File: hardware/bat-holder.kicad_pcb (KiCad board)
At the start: 2 copper layers, 85 x 56 mm, 113 parts, among them J101 BAT_1049P, J102 USB-A, K101 NTC, P101 BOOT, P102 DEBUG, P103 CON-SENSOR2, P104 C, P105 5V Out, P201 Input, Q101 BC846, Q102 BC846, Q103 DMP2035UVTQ, Q104 DMP2035UVTQ, Q201 Si4447ADY, U101 XMC1XXX24, U102 AP9211, U103 MAX17260_LS, U104 DRILL, U105 DRILL, U106 DRILL, U107 DRILL, U108 DRILL, U109 DRILL, U110 DRILL, U111 DRILL, U112 AP7333-33SA, U201 TPS61088RHL, U202 BD906XX-C-HRP7, U203 AAT3620

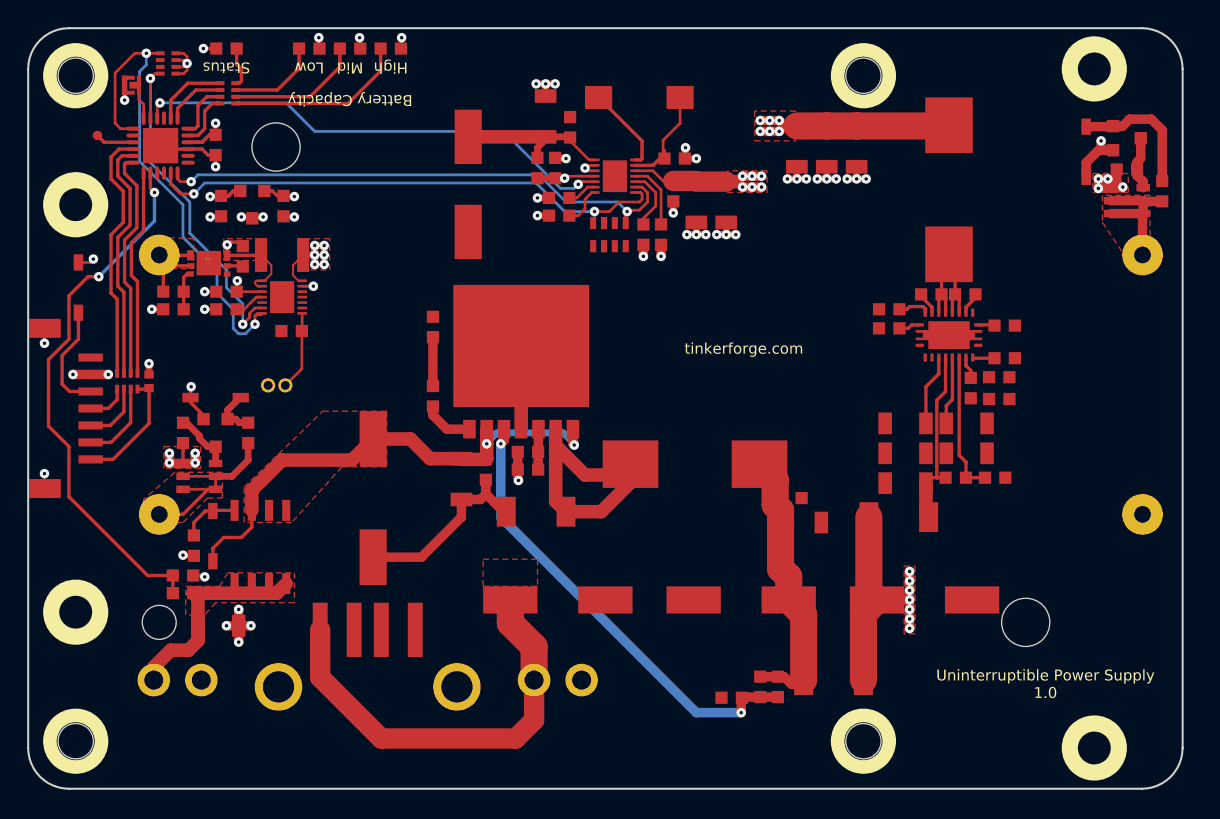
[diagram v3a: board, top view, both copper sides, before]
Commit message: fully routed
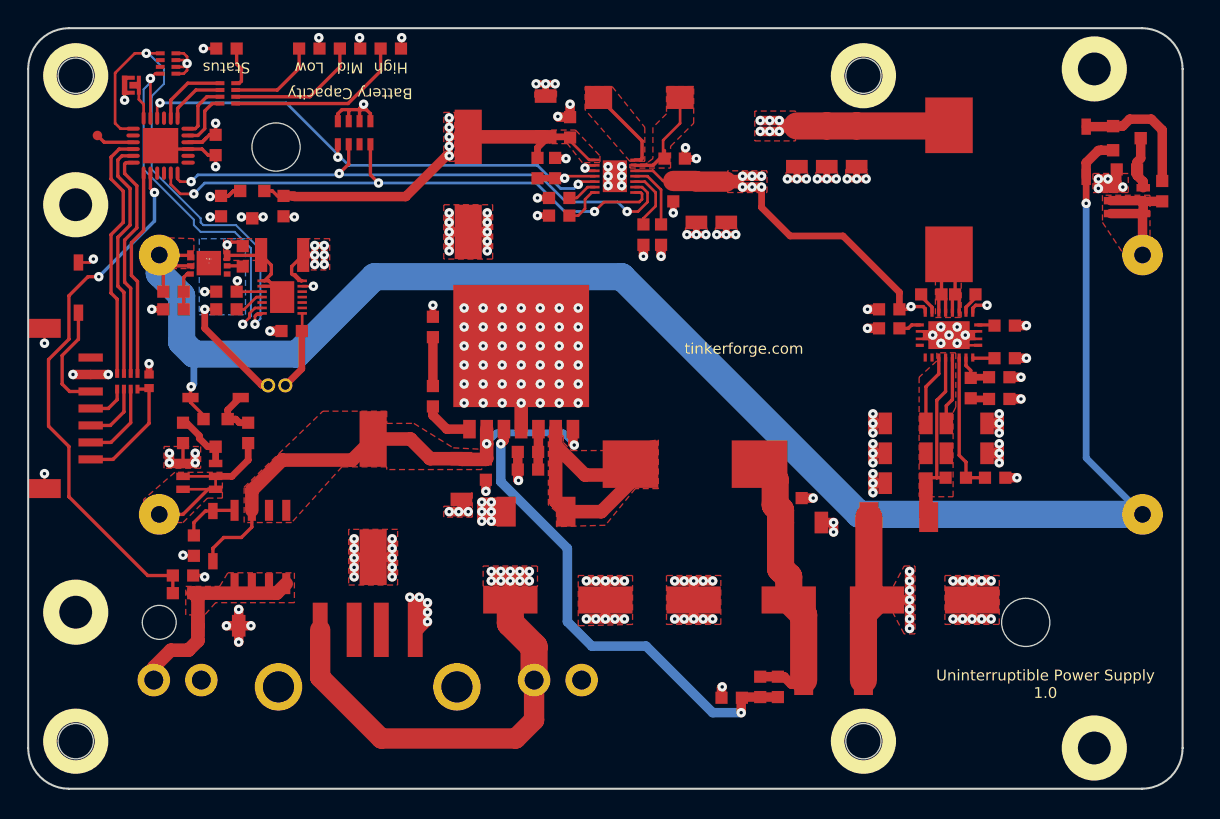
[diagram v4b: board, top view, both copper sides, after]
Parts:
- moved RP201 20.2 mm to (97.0, 83.7), turned to 0 degrees
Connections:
- net Net-(C207-Pad2) renamed CHG_IN
- net Net-(C214-Pad1) renamed 5VOUT
- net Net-(C228-Pad1) renamed L2
- net Net-(L203-Pad2) renamed L1
- RP201 pad 7: CHARGER_EN -> CHARGER_STAT1
- RP201 pad 8: CHARGER_STAT1 -> CHARGER_EN
- U203 pad EP: (no net) -> GND
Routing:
- net GND: track 75.1 -> 323.0 mm, vias 50 -> 199
- net BAT_OUT: track 45.9 -> 186.0 mm, vias 23 -> 26
- net GBAT: track 14.7 -> 130.8 mm
- net +5V: track 64.9 -> 156.4 mm, vias 8 -> 22
- net 3V3: track 17.3 -> 67.4 mm, vias 8 -> 9
- net VCC: track 5.39 -> 16.5 mm
- net AGND: track 10.3 -> 20.7 mm
- net BATTERY-SDA: track 26.8 -> 29.2 mm
- net CHARGER_STAT2: track 39.2 -> 41.5 mm, vias 2 -> 3
- net Net-(C227-Pad2): track 34.0 -> 35.7 mm
- net Net-(C213-Pad1): track 0.00 -> 1.37 mm
- net Net-(C212-Pad1): track 1.64 -> 3.02 mm
- net CHARGER_EN: track 36.0 -> 37.2 mm, vias 2 -> 3
- net CHARGER_STAT1: track 40.1 -> 41.1 mm, vias 2 -> 3
- added copper zone on VCC, net +5V
- added copper zone on VCC, net 3V3
- added copper zone on F.Cu, net 5VOUT
- added copper zone on B.Cu, net AGND
- added copper zone on VCC, net BAT_OUT
- added copper zone on F.Cu, net CHG_IN
- added copper zone on GND, net GND
- added copper zone on VCC, net GND
- added copper zone on F.Cu, net L1
- added copper zone on F.Cu, net L2
- added copper zone on F.Cu, net VSW
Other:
- copper layers 2 -> 4

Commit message: prototype finished
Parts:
- added Fiducial_Mark: VAL**, kicad-libraries:Fiducial_Mark, F.Cu at (75.0, 124.0)
- added Fiducial_Mark: VAL**, kicad-libraries:Fiducial_Mark, F.Cu at (156.0, 127.0)
- added Fiducial_Mark: VAL**, kicad-libraries:Fiducial_Mark, F.Cu at (146.0, 78.0)
- added Fiducial_Mark: VAL**, kicad-libraries:Fiducial_Mark, F.Cu at (75.0, 83.0)
- added G***: LOGO, kicad-libraries:Logo_31x31, F.Cu at (125.5, 96.4)
- added G***: LOGO, kicad-libraries:Logo_CoMCU, F.Cu at (150.2, 110.4)
- added VAL: CE_5mm, kicad-libraries:CE_5mm, F.Cu at (150.2, 96.0)
- added VAL: WEEE_7mm, kicad-libraries:WEEE_7mm, F.Cu at (150.2, 103.0)
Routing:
- added copper zone on B.Cu, net GND
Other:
- board text added: "Input"
- board text added: "Input 5-28VDC - +"
- board text added: "Output"

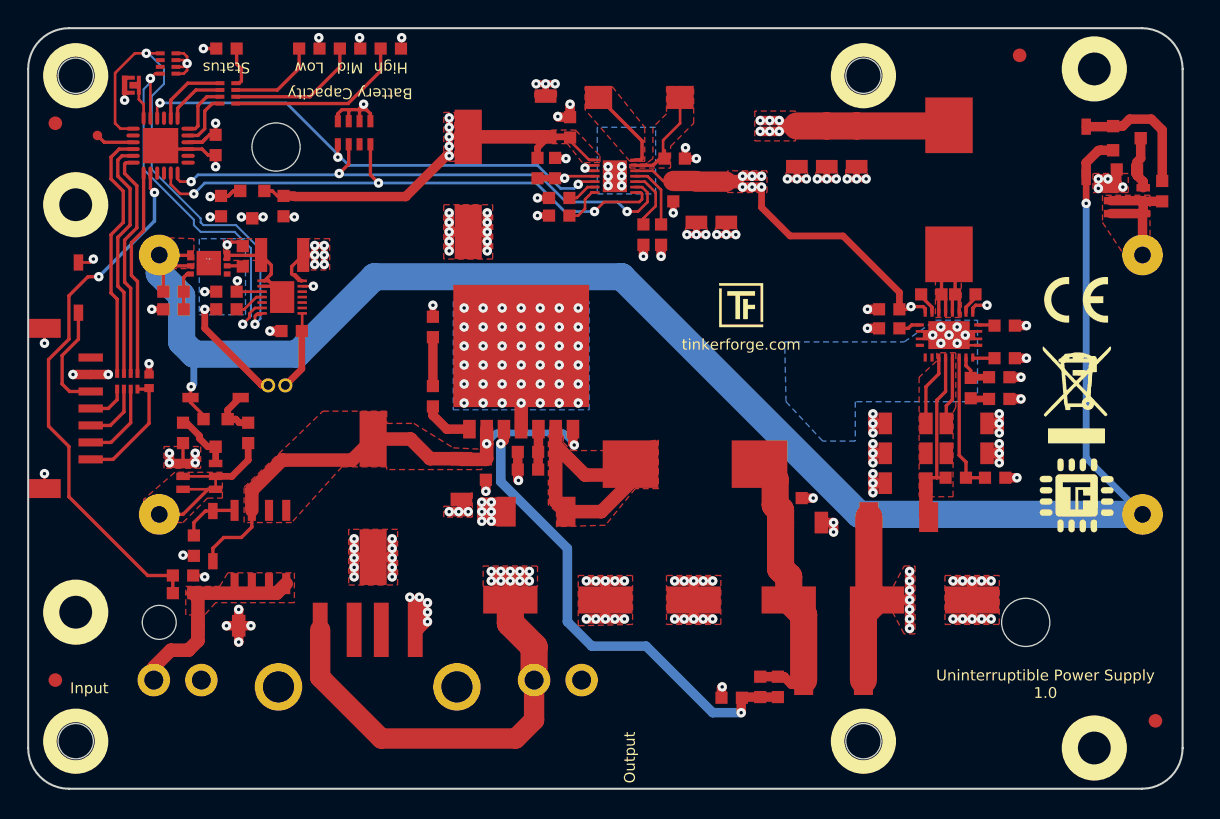
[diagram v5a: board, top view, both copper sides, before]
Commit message: fix diode footprint
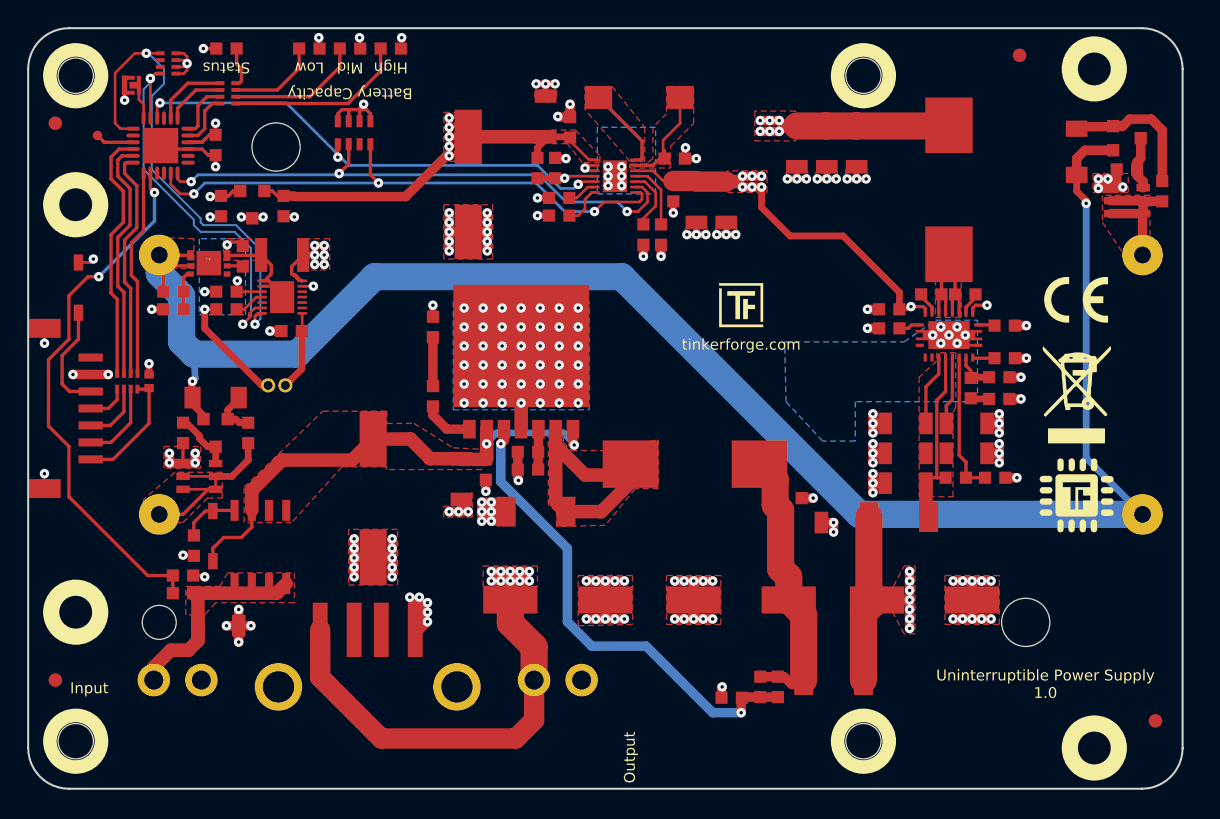
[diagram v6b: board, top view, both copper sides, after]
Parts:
- D101, D102: footprint SOD-123 -> MiniMelf
- moved D101 0.70 mm to (150.2, 85.1), turned to 270 degrees
- turned D102 to 180 degrees
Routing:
- net GBAT: track 130.8 -> 132.0 mm

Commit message: changed slikscreentext on bottomlayer <Output 5VDC>
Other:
- board text added: "Output 5VDC - +"
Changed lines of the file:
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@@
-(kicad_pcb (version 20171130) (host pcbnew 5.0.2-bee76a0~70~ubuntu18.04.1)
+(kicad_pcb (version 20171130) (host pcbnew 5.0.2-bee76a0~70~ubuntu18.10.1)
   (general
     (thickness 1.6)
@@
   )
   (setup
-    (last_trace_width 0.5)
+    (last_trace_width 0.15)
     (user_trace_width 0.2)
     (user_trace_width 0.25)
@@
     (effects (font (size 0.8 0.8) (thickness 0.15)))
   )
-  (gr_text "Input\n5-28VDC\n-    +" (at 112 127.9) (layer B.SilkS)
+  (gr_text "Output\n5VDC\n-    +" (at 112 127.9) (layer B.SilkS)
     (effects (font (size 1 1) (thickness 0.15)) (justify mirror))
   )

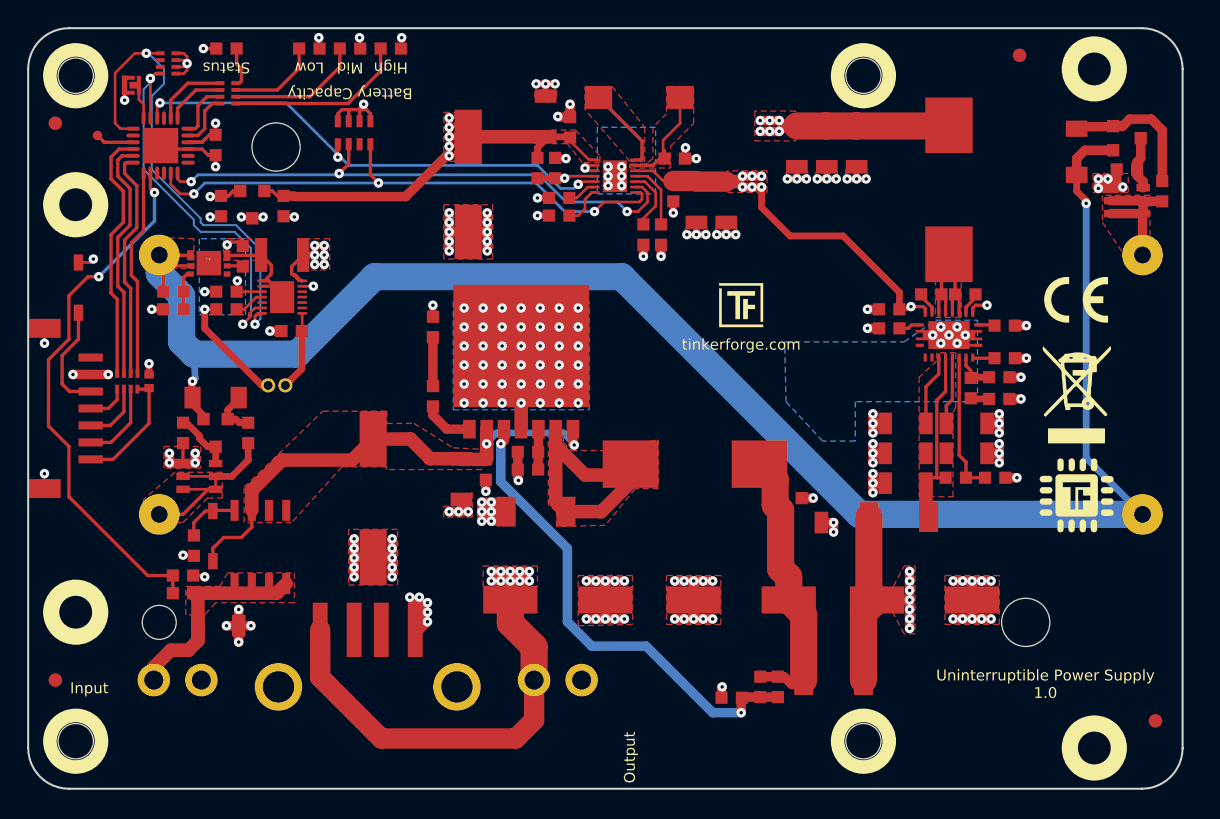
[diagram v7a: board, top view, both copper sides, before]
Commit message: added 0 ohm resistors and extented footprints for prototyping
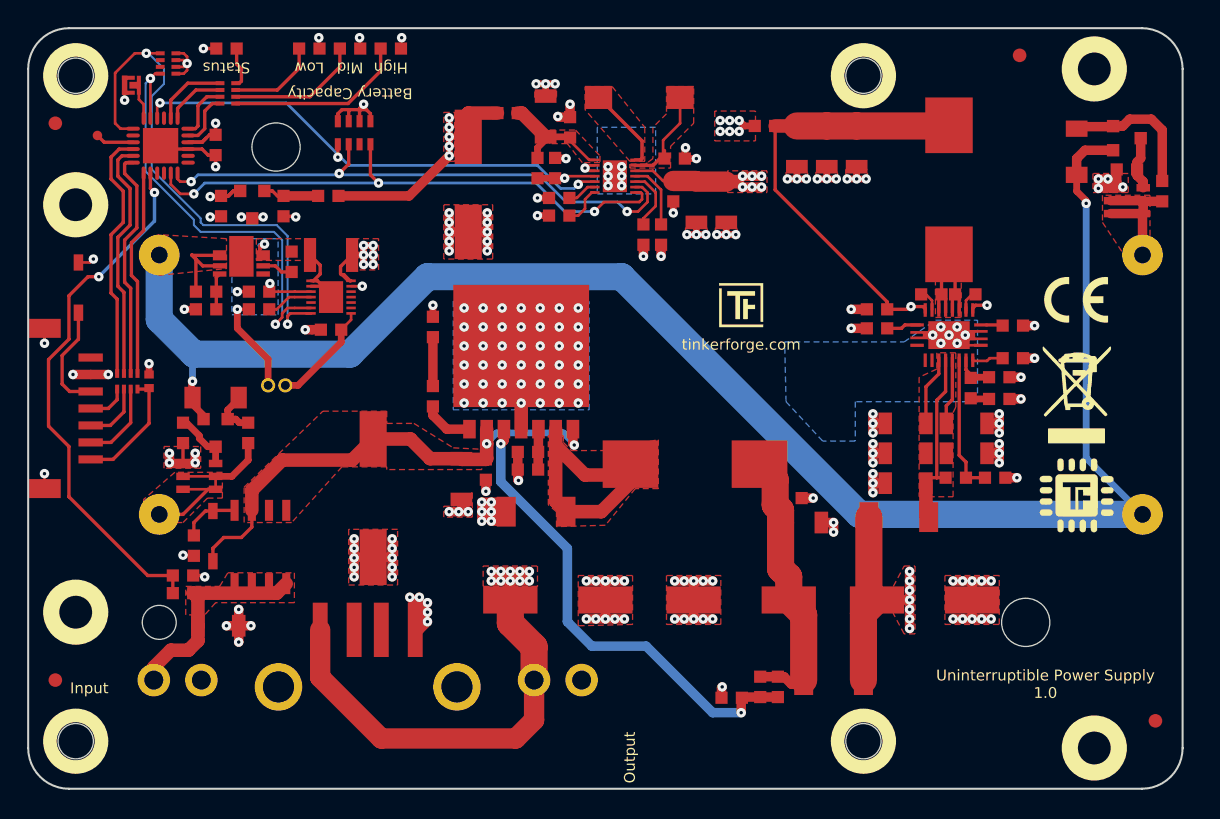
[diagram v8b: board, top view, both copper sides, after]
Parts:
- removed P104: C, TSTPT
- added R1: 0, kicad-libraries:R0603F, F.Cu at (95.1, 88.3)
- added R2: 0, kicad-libraries:R0603F, F.Cu at (127.2, 83.2)
- added R3: 0, kicad-libraries:R0603F, F.Cu at (108.3, 82.2)
- U102: footprint DFN2030-6 -> kicad-libraries:DFN2030-6
- U201: footprint VQFN20_45x35 -> kicad-libraries:VQFN20_45x35
- moved R108 3.62 mm to (92.4, 93.2)
- moved R110 3.60 mm to (95.3, 92.7)
- moved U103 3.60 mm to (95.3, 95.8)
- moved R109 2.90 mm to (95.3, 98.2)
- moved C104 2.40 mm to (90.0, 95.4)
- moved C105 2.40 mm to (90.0, 96.7)
- moved U102 2.40 mm to (88.7, 93.3)
- moved C102 2.40 mm to (86.1, 95.4)
- moved R107 2.40 mm to (86.1, 96.7)
- moved C204 0.90 mm to (135.5, 96.7)
- moved C210 0.90 mm to (135.5, 98.1)
- moved C205 0.60 mm to (145.5, 97.9)
- moved R206 0.60 mm to (145.5, 100.3)
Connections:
- C107 pad 2: +5V -> Net-(C107-Pad2)
- C201 pad 1: BAT_OUT -> Net-(C201-Pad1)
- C202 pad 1: BAT_OUT -> Net-(C201-Pad1)
- C203 pad 1: BAT_OUT -> Net-(C201-Pad1)
- C204 pad 1: BAT_OUT -> Net-(C201-Pad1)
- C221 pad 1: +5V -> Net-(C221-Pad1)
- C222 pad 1: +5V -> Net-(C221-Pad1)
- J102 pad 2: (no net) -> Net-(J102-Pad2)
- J102 pad 3: (no net) -> Net-(J102-Pad3)
- L201 pad 1: BAT_OUT -> Net-(C201-Pad1)
- P103 pad 1: (no net) -> Net-(P103-Pad1)
- R212 pad 1: +5V -> Net-(C221-Pad1)
- RP103 pad 2: (no net) -> Net-(RP103-Pad2)
- RP103 pad 3: (no net) -> Net-(RP103-Pad3)
- RP201 pad 6: (no net) -> Net-(RP201-Pad6)
- U101 pad 15: (no net) -> Net-(U101-Pad15)
- U101 pad 20: (no net) -> Net-(U101-Pad20)
- U101 pad 3: (no net) -> Net-(U101-Pad3)
- U101 pad 4: (no net) -> Net-(U101-Pad4)
- U101 pad 7: (no net) -> Net-(U101-Pad7)
- U101 pad 8: (no net) -> Net-(U101-Pad8)
- U102 pad 4: (no net) -> Net-(U102-Pad4)
- U103 pad 12: (no net) -> Net-(U103-Pad12)
- U103 pad 2: (no net) -> Net-(U103-Pad2)
- U103 pad 3: (no net) -> Net-(U103-Pad3)
- U103 pad 4: (no net) -> Net-(U103-Pad4)
- U103 pad 5: (no net) -> Net-(U103-Pad5)
- U112 pad 1: +5V -> Net-(C107-Pad2)
- U201 pad 11: (no net) -> Net-(U201-Pad11)
- U201 pad 12: (no net) -> Net-(U201-Pad12)
- U201 pad 13: (no net) -> Net-(U201-Pad13)
- U201 pad 2: BAT_OUT -> Net-(C201-Pad1)
- U201 pad 9: BAT_OUT -> Net-(C201-Pad1)
- U203 pad 1: +5V -> Net-(C221-Pad1)
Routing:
- net BAT_OUT: track 186.0 -> 132.1 mm, vias 26 -> 24
- net Net-(C201-Pad1): track 0.00 -> 40.1 mm, vias 0 -> 2
- net +5V: track 156.4 -> 142.6 mm
- net Net-(C221-Pad1): track 0.00 -> 9.05 mm
- net AGND: track 20.7 -> 16.6 mm
- net Net-(C107-Pad2): track 0.00 -> 4.11 mm
- net BATTERY-SDA: track 29.2 -> 32.9 mm
- net BATTERY-SCL: track 36.8 -> 40.3 mm
- net Net-(K101-Pad1): track 5.81 -> 7.85 mm
- net Net-(R108-Pad2): track 1.25 -> 2.54 mm
- net Net-(C105-Pad2): track 2.25 -> 3.45 mm
- net GND: track 323.0 -> 322.1 mm
- net Net-(C210-Pad1): track 1.60 -> 2.50 mm
- net Net-(R206-Pad1): track 1.62 -> 2.50 mm
- net Net-(R205-Pad1): track 1.64 -> 2.24 mm
- added copper zone on F.Cu, net Net-(C221-Pad1)
